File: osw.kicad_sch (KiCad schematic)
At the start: 60 parts, among them J1 Conn_01x02, J2 microSD_MEM2067-02-180-00-A_R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, J3 2169890001, Q1 Q_NMOS_ToshibaSMD, SW1 SPST_EVQ-P7J01P, SW2 SPST_EVQ-P7J01P, SW3 SPST_EVQ-P7J01P, SW4 SPST_EVQ-P7J01P, U1 L96-M33, U10 BMA400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

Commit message: Adding a few comments about what to use in the next gen.
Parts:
- U4: NOTE (none) -> USE DFN!!!
- U8: NOTE (none) -> USE TSSOP!!!
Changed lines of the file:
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@@
       (effects (font (size 1.2446 1.2446)) hide)
+    )
+    (property "NOTE" "USE DFN!!!" (at 35.56 247.65 0)
+      (effects (font (size 1.27 1.27)) hide)
     )
     (pin "1")
@@
       (effects (font (size 1.27 1.27)) (justify bottom) hide)
     )
-    (pin "1")
+    (property "NOTE" "USE TSSOP!!!" (at 175.26 76.2 0)
+      (effects (font (size 1.27 1.27)) hide)
+    )
+    (pin "1")

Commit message: Updates to a bunch of symbols and the entire schematic now matches the libs....  Now onto fixing the short.
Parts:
- D1: Manufacturer (none) -> Harvatek Corporation
- J2: Digikey_PN 2073-MEM2067-02-180-00-ACT-ND -> (none)
- SW1, SW2, SW3, SW4: Digikey_PN P16767CT-ND -> (none)
- U1: MNP L96-M33 -> (none)
- U13: Manufacturer (none) -> Rohm Semiconductor
- U3: MNP ESP32-MINI-1-N4 -> (none)
- U4: value MCP73831T-2ACI_OT -> MCP73831T-2ACI; footprint open-Smartwatch:SOT-23-5 -> Allard_dfn_qfn:PSON9P50_200X300X80L40X25T135X125L; DigiKey_PN MCP73831T-2ACI/OTCT-ND -> MCP73831T-2ACI/MCCT-ND; MPN MCP73831T-2ACI/OT -> MCP73831T-2ACI/MC; Mouser_PN 579-MCP73831T-2ACIOT -> 579-MCP73831T-2ACIMC; NOTE USE DFN!!! -> (none); manf# MCP73831T-2ACI/OT -> ${MPN}
- U8: footprint open-Smartwatch:SOIC127P600X175-8N_microchipRAM -> AllardSOP:SOP8P65_300X640X120L47X24N; DigiKey_PN 23K256T-I/SNCT-ND -> 23K256T-I/STCT-ND; MPN 23K256T-I/SN -> 23K256T-I/ST; NOTE USE TSSOP!!! -> (none); VDD_HIGH (none) -> 3.6; VDD_LOW (none) -> 2.7; manf# 23K256T-I/SN -> ${MPN}
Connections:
- net GND: now also U4.6 (VSS), U4.7 (NC), U4.9 (EP); no longer C8.2, U4.2 (VSS)
- net VBAT: now also U4.4 (VBAT)
- net VBUS: now also U4.1 (VDD), U4.2 (VDD); no longer U4.4 (VDD)
- net at D1.1 (K): now also U4.5 (STAT); no longer U4.1 (STAT)
- net at R13.1: now also U4.8 (PROG); no longer U4.5 (PROG)
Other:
- moved on the sheet: C15, C16, C17, C3, C6, C7, C8, R12, R18, R2, R3, R5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

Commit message: Updating some FPs.
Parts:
- C1, C17, C18: value cap0402_1p0u10V -> 1u; footprint open-Smartwatch:C_0402_1005Metric_osw -> AllardChip:CAPC100X50X60L25N; symbol open-Smartwatch:cap0402_1p0u10V -> AllardPassive:C10A72-10000; AI_PN (none) -> ${SYMBOL_NAME}; Capacitance 1.0u -> (none); DigiKey_PN 490-GRM155C81C105KE11JCT-ND -> 490-GRM155Z71A105KE01JCT-ND; ESR (none) -> X7R; MPN GRM155C81C105KE11J -> GRM155Z71A105KE01J; Mouser_PN 81-GRM155C81C105KE1J -> 81-GRM155Z71A105KE1J; SUP1 (none) -> Digi-Key; SUP1_PN (none) -> 490-GRM155Z71A105KE01JCT-ND; SUP2 (none) -> Mouser; SUP2_PN (none) -> 81-GRM155Z71A105KE1J; Temperature (none) -> -55-125; Tolerance (none) -> 10%; Voltage 16V -> 10V; manf# GRM155C81C105KE11J -> ${MPN}; variant (none) -> default
- C12, C15, C16, C2, C5, C6, C7, C8, C9: value cap0402_p1u10V -> 100n; footprint open-Smartwatch:C_0402_1005Metric_osw -> AllardChip:CAPC100X50X55L25N; symbol open-Smartwatch:cap0402_p1u10V -> AllardPassive:C10A82-10000; AI_PN (none) -> ${SYMBOL_NAME}; Capacitance 0.1u -> (none); DigiKey_PN 13-CC0402KPX5R6BB104CT-ND -> 490-13342-1-ND; ESR (none) -> X7R; MPN CC0402KPX5R6BB104 -> GRM155R71H104KE14J; Manufacturer YAGEO -> Murata Electronics; Mouser_PN 603-CC402KPX5R6BB104 -> 81-GRM155R71H104KE4J; SUP1 (none) -> Digi-Key; SUP1_PN (none) -> 490-13342-1-ND; SUP2 (none) -> Mouser; SUP2_PN (none) -> 81-GRM155R71H104KE4J; Temperature (none) -> -55-125; Tolerance (none) -> 10%; Voltage 10V -> 50V; manf# CC0402KPX5R6BB104 -> ${MPN}; variant (none) -> default
- R10, R11, R13, R16, R17, R20, R21, R4, R6, R7, R8, R9: value res0402_10k -> 10k; footprint open-Smartwatch:R_0402_1005Metric_osw -> AllardChip:RESC100X50X40L25N; symbol open-Smartwatch:res0402_10k -> AllardPassive:R10022-10000; AI_PN (none) -> ${SYMBOL_NAME}; DigiKey_PN 13-RC0402DR-0710KLCT-ND -> P10.0KLCT-ND; MPN RC0402DR-0710KL -> ERJ-2RKF1002X; Manufacturer YAGEO -> Panasonic Electronics Components; Mouser_PN 603-RC0402DR-0710KL -> 667-ERJ-2RKF1002X; Power (none) -> 0.1W; Resistance 10k -> (none); SUP1 (none) -> Digi-Key; SUP1_PN (none) -> P10.0KLCT-ND; SUP2 (none) -> Mouser; SUP2_PN (none) -> 667-ERJ-2RKF1002X; Temperature (none) -> -55-155; Tolerance (none) -> 1%; manf# RC0402DR-0710KL -> ${MPN}; variant (none) -> default
- R12, R2, R3, R5: value res0402_1k -> 1k; footprint open-Smartwatch:R_0402_1005Metric_osw -> AllardChip:RESC100X50X40L25N; symbol open-Smartwatch:res0402_1k -> AllardPassive:R10012-10000; AI_PN (none) -> ${SYMBOL_NAME}; DigiKey_PN 311-1.0KJRCT-ND -> P1.00KLCT-ND; MPN RC0402JR-071KL -> ERJ-2RKF1001X; Manufacturer YAGEO -> Panasonic Electronics Components; Mouser_PN 603-RC0402JR-071KL -> 667-ERJ-2RKF1001X; Power (none) -> 0.1W; Resistance 1k -> (none); SUP1 (none) -> Digi-Key; SUP1_PN (none) -> P1.00KLCT-ND; SUP2 (none) -> Mouser; SUP2_PN (none) -> 667-ERJ-2RKF1001X; Temperature (none) -> -55-155; Tolerance (none) -> 1%; manf# RC0402JR-071KL -> ${MPN}; variant (none) -> default
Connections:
- net GND: now also C8.2
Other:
- moved on the sheet: C1, C12, C15, C16, C17, C18, C2, C5, C6, C7, C8, C9

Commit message: Updates.
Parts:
- U8: value 23K256-I/SN -> 23K256T-I/ST; footprint AllardSOP:SOP8P65_300X640X120L47X24N -> AllardSOP:SOP8P65_300X640X120L47X24L
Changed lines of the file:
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@@
     (stroke (width 0) (type default))
   )
-  (polyline (pts (xy 77.47 63.5) (xy 77.77 147))
+  (polyline (pts (xy 77.47 63.5) (xy 77.47 146.05))
     (stroke (width 0) (type default))
   )
@@
     (stroke (width 0) (type default))
   )
-  (polyline (pts (xy 12.7 63.5) (xy 76.835 63.5))
+  (polyline (pts (xy 12.7 63.5) (xy 77.47 63.5))
     (stroke (width 0) (type default))
   )
@@
     (stroke (width 0) (type default))
   )
-  (polyline (pts (xy 77.77 147) (xy 13 147))
+  (polyline (pts (xy 77.47 146.05) (xy 12.7 146.05))
     (stroke (width 0) (type default))
   )
@@
     (stroke (width 0) (type default))
   )
-  (polyline (pts (xy 13 147) (xy 12.7 63.5))
+  (polyline (pts (xy 12.7 146.05) (xy 12.7 63.5))
     (stroke (width 0) (type default))
   )
@@
       (effects (font (size 1.27 1.27)))
     )
-    (property "Value" "23K256-I/SN" (at 177.8 66.04 0)
+    (property "Value" "23K256T-I/ST" (at 177.8 66.04 0)
       (effects (font (size 1.27 1.27)))
     )
-    (property "Footprint" "AllardSOP:SOP8P65_300X640X120L47X24N" (at 173.26 98.2 0)
+    (property "Footprint" "AllardSOP:SOP8P65_300X640X120L47X24L" (at 173.26 98.2 0)
       (effects (font (size 1.27 1.27)) (justify bottom) hide)
     )

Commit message: Updating the FP for a SOT23.
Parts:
- Q1: footprint open-Smartwatch:SOT95P247X115-3N -> AllardSOT:SOT23-3P95_240X105L35X42L

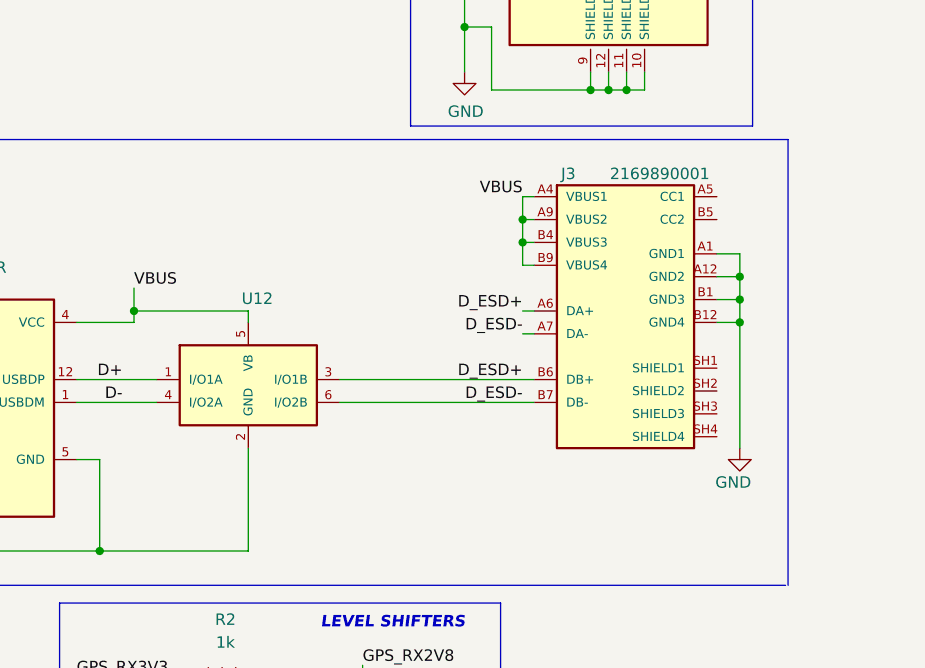
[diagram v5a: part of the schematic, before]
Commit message: Got USB connector chagned.
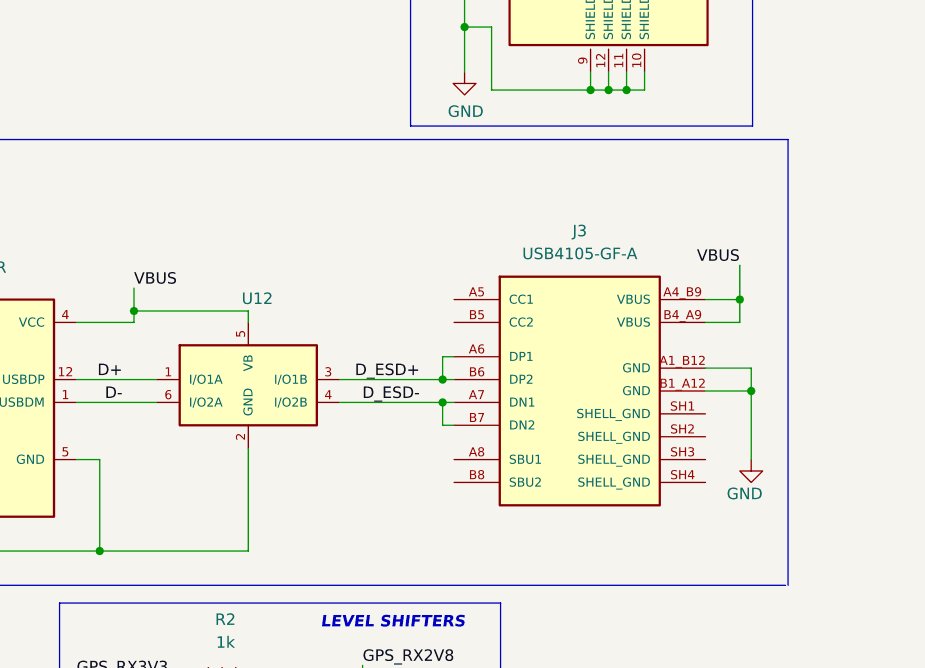
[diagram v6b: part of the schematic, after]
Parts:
- removed J3: 2169890001, open-Smartwatch:MOLEX_2169890001, symbol open-Smartwatch:Molex_2169890001
- added J3: USB4105-GF-A, AllardConnFootPrints:GCT_USB4105-GF-A, symbol AllardConn:J10021
- U12: footprint open-Smartwatch:SOT-457_ESD -> AllardSOT:SOT23-6P95_275X110L45X32N; manf# IP4234CZ6,125 -> ${MPN}
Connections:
- net D-: now also U12.6 (I/O2A); no longer U12.4 (I/O2A)
- net D_ESD+: now also J3.A6 (DP1), J3.B6 (DP2)
- net D_ESD-: now also U12.4 (I/O2B), J3.A7 (DN1), J3.B7 (DN2); no longer U12.6 (I/O2B)
- net GND: now also J3.A1_B12 (GND), J3.B1_A12 (GND)
- net VBUS: now also J3.A4_B9 (VBUS), J3.B4_A9 (VBUS)
